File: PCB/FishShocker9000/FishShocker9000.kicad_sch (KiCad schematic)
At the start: 54 parts, among them J1 Barrel_Jack, Q1 AO3401A, U1 MP2331HGTL-Z, U2 SN754410NE, U3 DEV-16771, U4 OPA2197xD, U5 OPA2197xD, U6 OPA2197xD, U7 OPA2197xD, U8 OPA2197xD, U9 OPA2197xD

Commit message: Added values to passive components. Need to add various footprints and change pmos transistor to FQP47P06.
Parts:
- added D10, D11, D12, D13, D2, D3, D4, D5, D6, D7, D8, D9: GREEN, symbol Device:LED
- added R33, R34, R35, R36, R37, R38, R39, R40, R41, R42, R43: 220, symbol Device:R_Small
- added U10, U11, U12, U13, U14: SN754410NE, Package_DIP:DIP-16_W7.62mm, symbol Driver_Motor:SN754410NE
- C10: value C_Small -> 0u1
- C3: value C_Small -> 1n
- C4: value C_Small -> 6n8
- C5: value C_Small -> 1u
- C6, C7, C9: value C_Small -> 22u
- C8: value C_Small -> 10p
- D1: value RED -> GREEN
- L1: value L_Small -> 3u3
- R1, R5: value R_Small -> 10k
- R10, R12, R14, R16, R17, R20, R21, R24, R26, R28, R30, R8: value R_Small -> 3.3k
- R11, R13, R15, R18, R19, R22, R23, R25, R27, R29, R31, R9: value R_Small -> 15k
- R2: value R_Small -> 20
- R3: value R_Small -> 40k2
- R32: value 10k -> 220
- R4: value R_Small -> 7k68
- R7: value 330 -> 220
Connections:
- net A0: now also R32.1; no longer U5.3 (+), U6.3 (+), U7.3 (+), U8.3 (+), U9.3 (+)
- net A1: now also R34.1; no longer U5.5 (+), U6.5 (+), U7.5 (+), U8.5 (+), U9.5 (+)
- net A10: now also U9.3 (+), R39.1
- net A11: now also U9.5 (+), R43.1
- net A2: now also U5.3 (+), R33.1
- net A3: now also U5.5 (+), R35.1
- net A4: now also U6.3 (+), R36.1
- net A5: now also U6.5 (+), R40.1
- net A6: now also U7.3 (+), R37.1
- net A7: now also U7.5 (+), R41.1
- net A8: now also U8.3 (+), R38.1
- net A9: now also U8.5 (+), R42.1
- net BUCK_VOUT: now also U2.8 (VCC2), U10.16 (VCC1), U10.8 (VCC2), U11.16 (VCC1), U11.8 (VCC2), U12.16 (VCC1), U12.8 (VCC2), U13.16 (VCC1), U13.8 (VCC2), U14.16 (VCC1), U14.8 (VCC2); no longer R32.1
- net CELL1: now also U2.2 (1A)
- net CELL10: now also U13.10 (3A)
- net CELL11: now also U14.2 (1A)
- net CELL12: now also U14.10 (3A)
- net CELL2: now also U2.10 (3A)
- net CELL3: now also U10.2 (1A)
- net CELL4: now also U10.10 (3A)
- net CELL5: now also U11.2 (1A)
- net CELL6: now also U11.10 (3A)
- net CELL7: now also U12.2 (1A)
- net CELL8: now also U12.10 (3A)
- net CELL9: now also U13.2 (1A)
- net GND: now also U2.15 (4A), U2.7 (2A), D10.1 (K), D11.1 (K), D12.1 (K), D13.1 (K), D2.1 (K), D3.1 (K), D4.1 (K), D5.1 (K), D6.1 (K), D7.1 (K), D8.1 (K), D9.1 (K), U10.12 (GND), U10.13 (GND), U10.15 (4A), U10.4 (GND), U10.5 (GND), U10.7 (2A), U11.12 (GND), U11.13 (GND), U11.15 (4A), U11.4 (GND), U11.5 (GND), U11.7 (2A), U12.12 (GND), U12.13 (GND), U12.15 (4A), U12.4 (GND), U12.5 (GND), U12.7 (2A), U13.12 (GND), U13.13 (GND), U13.15 (4A), U13.4 (GND), U13.5 (GND), U13.7 (2A), U14.12 (GND), U14.13 (GND), U14.15 (4A), U14.4 (GND), U14.5 (GND), U14.7 (2A)
- net at R32.2: now also D2.2 (A); no longer U2.1 (1,2EN)
- net Plate 2.1: now reaches U2.11 (3Y)
- net Plate 2.2: now reaches U2.14 (4Y)
- net Plate 1.1: now reaches U2.3 (1Y)
- net Plate 1.2: now reaches U2.6 (2Y)
- new net: D10.2 (A), R40.2
- new net: D11.2 (A), R41.2
- new net: D13.2 (A), R43.2
- new net: D5.2 (A), R35.2
- new net: D4.2 (A), R34.2
- new net: D8.2 (A), R38.2
- new net: D3.2 (A), R33.2
- new net: D7.2 (A), R37.2
- new net: D9.2 (A), R39.2
- new net: D6.2 (A), R36.2
- new net: D12.2 (A), R42.2
- new net Plate 10.1: U13.11 (3Y)
- new net Plate 10.2: U13.14 (4Y)
- new net Plate 11.1: U14.3 (1Y)
- new net Plate 11.2: U14.6 (2Y)
- new net Plate 12.1: U14.11 (3Y)
- new net Plate 12.2: U14.14 (4Y)
- new net Plate 3.1: U10.3 (1Y)
- new net Plate 3.2: U10.6 (2Y)
- new net Plate 4.1: U10.11 (3Y)
- new net Plate 4.2: U10.14 (4Y)
- new net Plate 5.1: U11.3 (1Y)
- new net Plate 5.2: U11.6 (2Y)
- new net Plate 6.1: U11.11 (3Y)
- new net Plate 6.2: U11.14 (4Y)
- new net Plate 7.1: U12.3 (1Y)
- new net Plate 7.2: U12.6 (2Y)
- new net Plate 8.1: U12.11 (3Y)
- new net Plate 8.2: U12.14 (4Y)
- new net Plate 9.1: U13.3 (1Y)
- new net Plate 9.2: U13.6 (2Y)
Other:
- note added: "H-Bridges"
- note added: "POWER VERIFICATION LED ON = GOOD POWER"
- note removed: "POWER VERIFICATION LED ON = BAD POWER"
- moved on the sheet: C6, R12, R13, R16, R17, R18, R19, R24, R25, R28, R29, R8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

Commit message: Added CAN Bus Tranciever and Pogo Pins
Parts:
- removed Q1: AO3401A, Package_TO_SOT_SMD:SOT-23, symbol Transistor_FET:AO3401A
- added J10, J11, J12, J13, J14, J15, J16, J17, J18, J19, J2, J20, J21, J22, J23, J24, J25, J26, J27, J28, J29, J3, J30, J31, J32, J33, J34, J35, J36, J37, J38, J39, J4, J40, J41, J42, J43, J44, J45, J46, J47, J48, J49, J5, J50, J51, J52, J53, J54, J55, J56, J57, J58, J59, J6, J60, J61, J62, J63, J64, J65, J66, J67, J68, J69, J7, J70, J71, J72, J73, J74, J8, J9: P70-1000045R, P70-1000045R:HARWIN_P70-1000045R, symbol P70-1000045R:P70-1000045R
- added J75: Screw_Terminal_01x02, symbol Connector:Screw_Terminal_01x02
- added Q2: FQP27P06, Package_TO_SOT_THT:TO-220-3_Vertical, symbol Transistor_FET:FQP27P06
- added U15: TCAN334, symbol Interface_CAN_LIN:TCAN334
- FB1: value FerriteBead_Small -> 600 @ 600 MHz
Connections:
- net GND: now also U3.GND1 (GND), U3.GND2 (GND), U3.GND3 (GND), U3.GND4 (GND), U3.GND5 (GND), U3.USB_GND1 (USB_GND), U3.USB_GND2 (USB_GND), Q2.1 (G), U15.2 (GND), U15.5 (SHDN), U15.8 (STB)
- net Plate 1.1: now also J6.1, J7.1, J8.1
- net Plate 1.2: now also J3.1, J4.1, J5.1
- net Plate 10.1: now also J64.1, J68.1, J72.1
- net Plate 10.2: now also J63.1, J67.1, J71.1
- net Plate 11.1: now also J54.1, J58.1, J62.1
- net Plate 11.2: now also J53.1, J57.1, J61.1
- net Plate 12.1: now also J66.1, J70.1, J74.1
- net Plate 12.2: now also J65.1, J69.1, J73.1
- net Plate 2.1: now also J16.1, J20.1, J24.1
- net Plate 2.2: now also J15.1, J19.1, J23.1
- net Plate 3.1: now also J10.1, J12.1, J14.1
- net Plate 3.2: now also J11.1, J13.1, J9.1
- net Plate 4.1: now also J18.1, J22.1, J26.1
- net Plate 4.2: now also J17.1, J21.1, J25.1
- net Plate 5.1: now also J28.1, J32.1, J36.1
- net Plate 5.2: now also J27.1, J31.1, J35.1
- net Plate 6.1: now also J40.1, J44.1, J48.1
- net Plate 6.2: now also J39.1, J43.1, J47.1
- net Plate 7.1: now also J30.1, J34.1, J38.1
- net Plate 7.2: now also J29.1, J33.1, J37.1
- net Plate 8.1: now also J42.1, J46.1, J50.1
- net Plate 8.2: now also J41.1, J45.1, J49.1
- net Plate 9.1: now also J52.1, J56.1, J60.1
- net Plate 9.2: now also J51.1, J55.1, J59.1
- net Polarity Enable 1: now also U10.1 (1,2EN), U11.1 (1,2EN), U12.1 (1,2EN), U13.1 (1,2EN), U14.1 (1,2EN), U2.1 (1,2EN)
- net Polarity Enable 2: now also U10.9 (3,4EN), U11.9 (3,4EN), U12.9 (3,4EN), U13.9 (3,4EN), U14.9 (3,4EN), U2.9 (3,4EN)
- net VCC: now also Q2.2 (D); no longer C10.1, C9.1, FB1.1, FB1.2, R6.2, U1.2 (IN), U4.8 (V+), U5.8 (V+), U6.8 (V+), U7.8 (V+), U8.8 (V+), U9.8 (V+)
- net 3.3v: now reaches U3.3.3V_1 (3.3V), U3.3.3V_2 (3.3V), U3.3.3V_3 (3.3V)
- net 3.3v: now also U15.3 (VCC)
- net RXD: now reaches U3.30 (CRX3)
- net RXD: now also U15.4 (RXD)
- net TXD: now reaches U3.31 (CTX3)
- net TXD: now also U15.1 (TXD)
- new net: J75.2 (Pin_2), U15.6 (CANL)
- new net: J75.1 (Pin_1), U15.7 (CANH)
- new net: FB1.1, Q2.3 (S)
- new net AMP_RAIL: C10.1, C9.1, FB1.2, R6.2, U1.2 (IN), U4.8 (V+), U5.8 (V+), U6.8 (V+), U7.8 (V+), U8.8 (V+), U9.8 (V+)
- no-connect marks 0 -> 37
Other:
- note added: "CAN Bus"
- note added: "Pogo Pin Connections (6 per Y, 3 per "side")"
- moved on the sheet: C3, FB1

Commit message: Made general layout for PCB
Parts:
- removed J2: P70-1000045R, P70-1000045R:HARWIN_P70-1000045R, symbol P70-1000045R:P70-1000045R
- removed U1: MP2331HGTL-Z, SOT583_MP2331H, symbol MP23315:MP2331HGTL-Z
- added H1, H2, H3, H4: MountingHole_Pad, MountingHole:MountingHole_4.3mm_M4_Pad, symbol Mechanical:MountingHole_Pad
- added U16: MP2331HGTL-Z, Library:SOT583_MP2331H, symbol MP2331HGTL-Z:MP2331HGTL-Z
- C10, C4: footprint (none) -> Capacitor_SMD:C_0603_1608Metric
- C3: footprint (none) -> Capacitor_SMD:C_0402_1005Metric
- C5, C6, C7, C9: footprint (none) -> Capacitor_SMD:C_1206_3216Metric
- C8: footprint (none) -> Capacitor_SMD:C_0201_0603Metric
- D1, D10, D11, D12, D13, D2, D3, D4, D5, D6, D7, D8, D9: footprint (none) -> LED_SMD:LED_0805_2012Metric
- FB1, L1: footprint (none) -> Inductor_SMD:L_0805_2012Metric
- J1: footprint (none) -> Connector_BarrelJack:BarrelJack_CLIFF_FC681465S_SMT_Horizontal
- J10, J11, J12, J13, J14, J15, J16, J17, J18, J19, J20, J21, J22, J23, J24, J25, J26, J27, J28, J29, J3, J30, J31, J32, J33, J34, J35, J36, J37, J38, J39, J4, J40, J41, J42, J43, J44, J45, J46, J47, J48, J49, J5, J50, J51, J52, J53, J54, J55, J56, J57, J58, J59, J6, J60, J61, J62, J63, J64, J65, J66, J67, J68, J69, J7, J70, J71, J72, J73, J74, J8, J9: footprint P70-1000045R:HARWIN_P70-1000045R -> Library:HARWIN_P70-1000045R
- J75: footprint (none) -> TerminalBlock:TerminalBlock_Altech_AK300-2_P5.00mm
- R1, R10, R11, R12, R13, R14, R15, R16, R17, R18, R19, R2, R20, R21, R22, R23, R24, R25, R26, R27, R28, R29, R3, R30, R31, R32, R33, R34, R35, R36, R37, R38, R39, R4, R40, R41, R42, R43, R5, R6, R7, R8, R9: footprint (none) -> Resistor_SMD:R_0805_2012Metric
- U15: footprint (none) -> Library:D0008A_L
- U3: footprint DEV-16771:MODULE_DEV-16771 -> Library:Teensy 4.1
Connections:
- net EN is gone; now on net BUCK_EN: R6.1
- net AMP_RAIL: now also U16.2 (IN)
- net BUCK_BST: now also U16.5 (BST)
- net BUCK_EN: now also U16.6 (EN)
- net BUCK_FB: now also U16.8 (FB)
- net BUCK_PG: now also U16.1 (PG)
- net BUCK_SS: now also U16.7 (SS)
- net BUCK_SW: now also U16.3 (SW)
- net GND: now also H1.1, H2.1, H3.1, H4.1, U16.4 (GND)
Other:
- note added: "Pogo Pin Connections (6 per Y, 2 per arm (3 arms))"
- note added: "TODO: CHECK???"
- note removed: "Pogo Pin Connections (6 per Y, 3 per "side")"
- note removed: "TODO: Figure out Values for all placeholders"

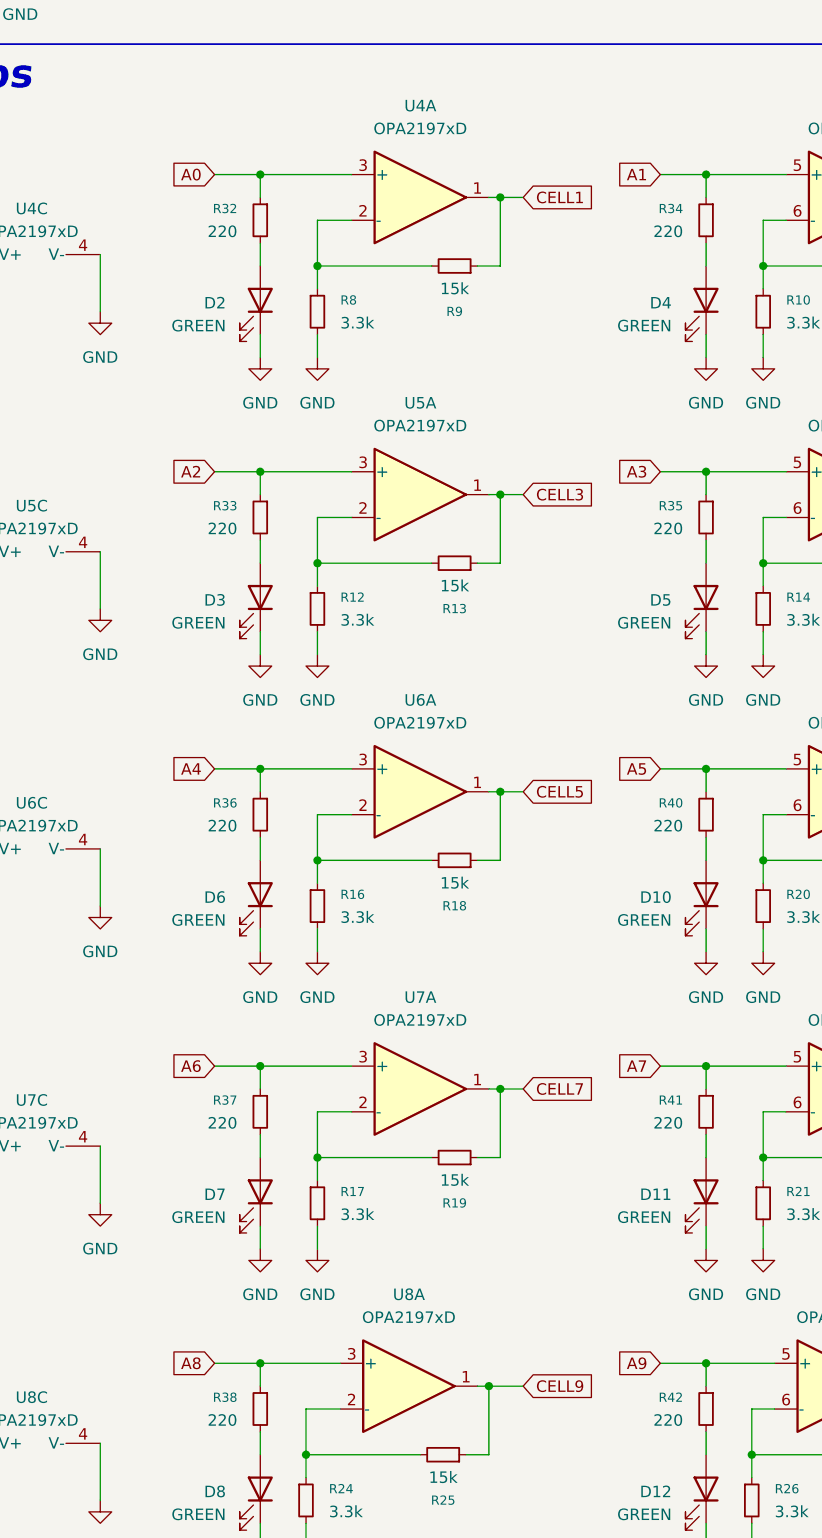
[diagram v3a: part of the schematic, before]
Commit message: routed PCB except for GND and Pogo Pins
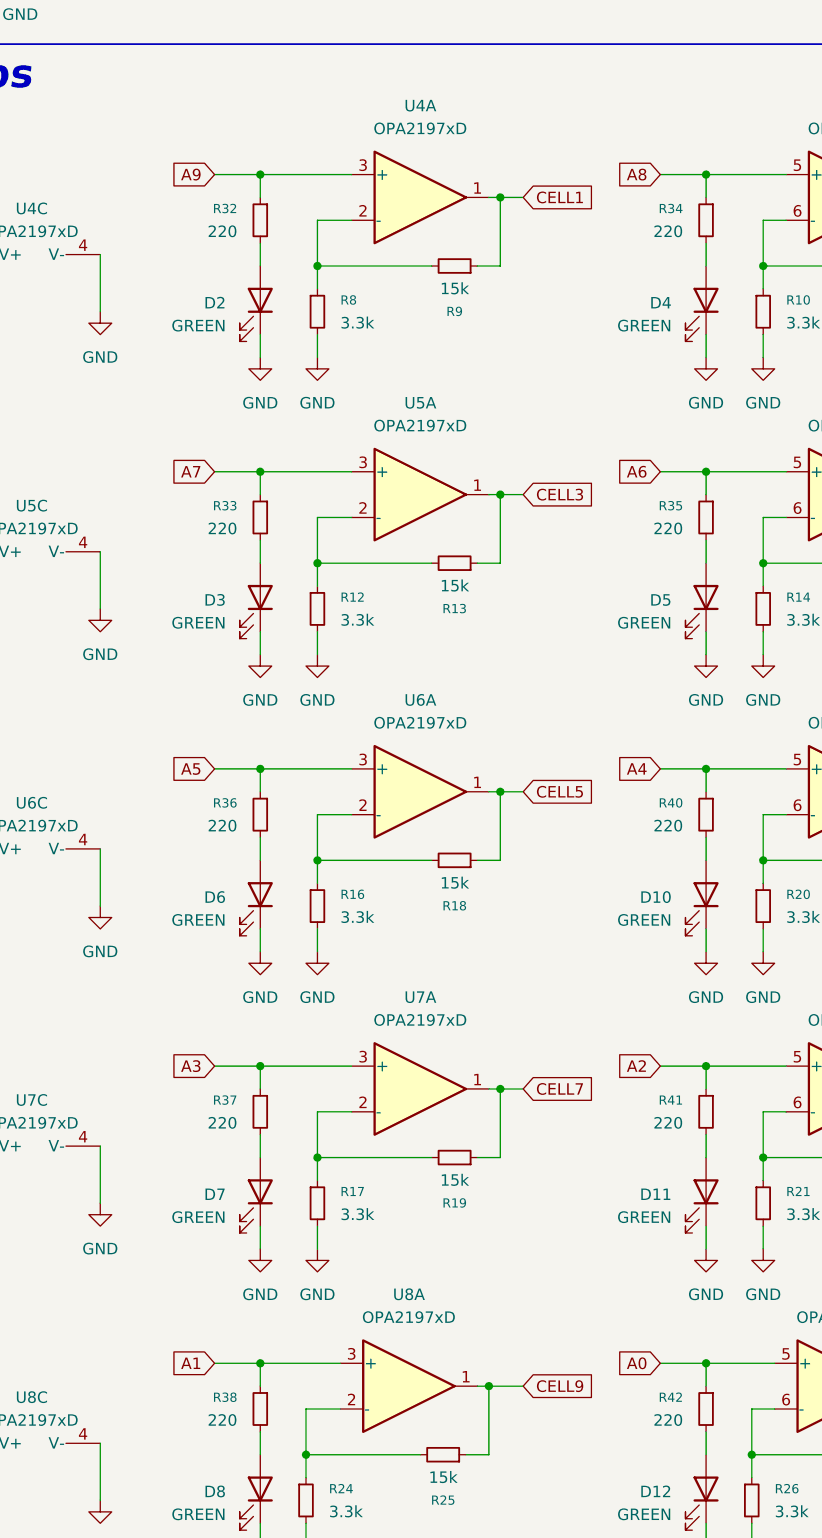
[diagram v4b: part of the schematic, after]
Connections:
- net A0: now also R42.1, U8.5 (+); no longer R32.1, U4.3 (+)
- net A1: now also R38.1, U8.3 (+); no longer R34.1, U4.5 (+)
- net A2: now also R41.1, U7.5 (+); no longer R33.1, U5.3 (+)
- net A3: now also R37.1, U7.3 (+); no longer R35.1, U5.5 (+)
- net A4: now also R40.1, U6.5 (+); no longer R36.1, U6.3 (+)
- net A5: now also R36.1, U6.3 (+); no longer R40.1, U6.5 (+)
- net A6: now also R35.1, U5.5 (+); no longer R37.1, U7.3 (+)
- net A7: now also R33.1, U5.3 (+); no longer R41.1, U7.5 (+)
- net A8: now also R34.1, U4.5 (+); no longer R38.1, U8.3 (+)
- net A9: now also R32.1, U4.3 (+); no longer R42.1, U8.5 (+)
